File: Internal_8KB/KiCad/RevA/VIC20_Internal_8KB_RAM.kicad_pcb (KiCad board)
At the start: 2 copper layers, 70 x 60 mm, 10 parts, among them J1 UD4, J2 UE4, J3 SW, J4 Signals, U1 6264, U2 GAL16V8

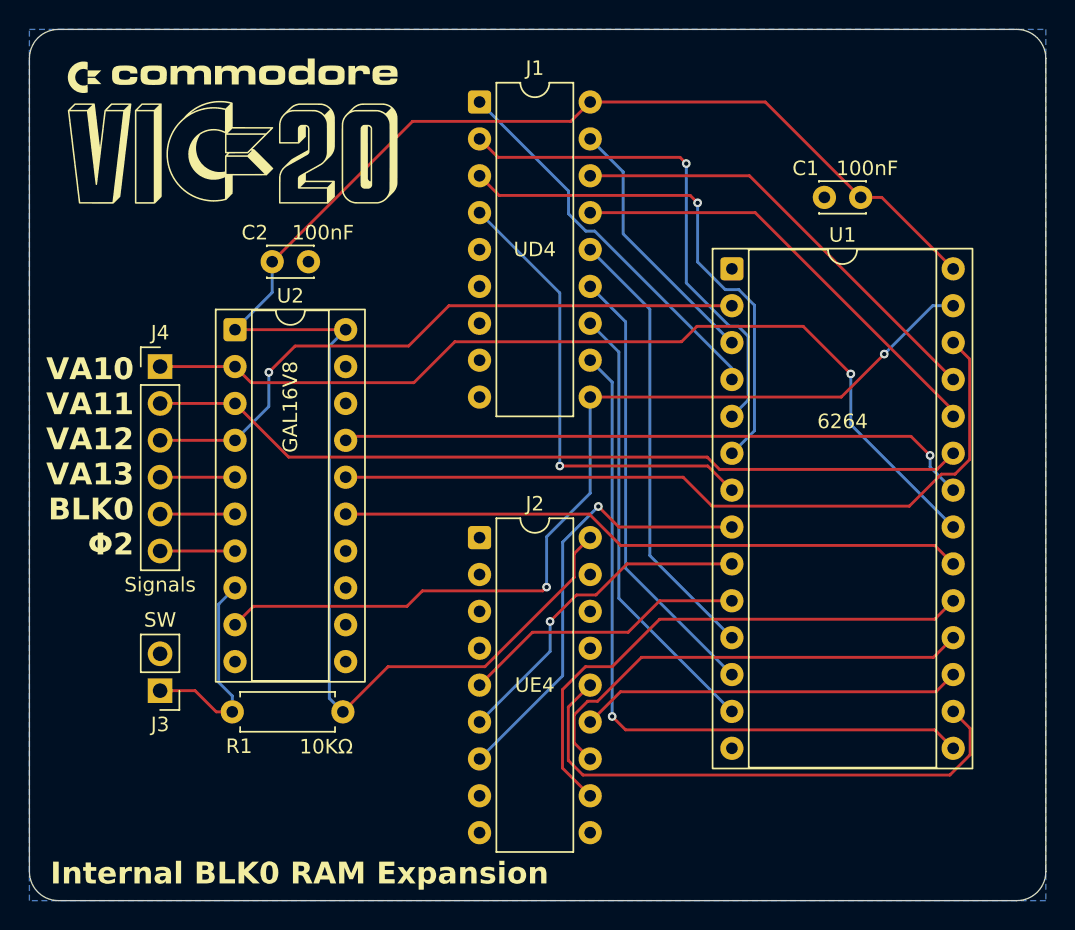
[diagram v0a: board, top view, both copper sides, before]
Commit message: Minor track routing changes
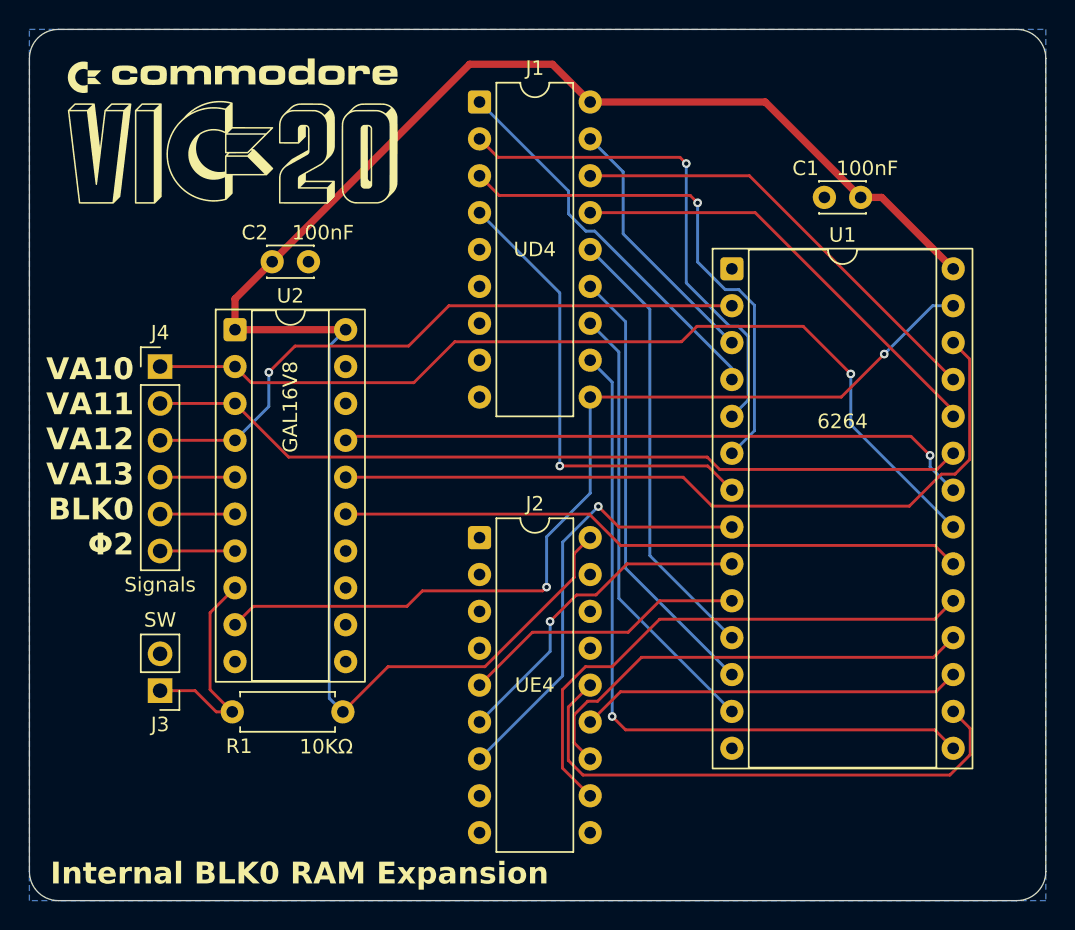
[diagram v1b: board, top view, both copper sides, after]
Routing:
- net +5V: track 119.7 -> 121.9 mm
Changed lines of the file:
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@@
 		(embedded_fonts no)
 		(model "${KICAD9_3DMODEL_DIR}/Package_DIP.3dshapes/DIP-18_W7.62mm.wrl"
+			(hide yes)
 			(offset
 				(xyz 0 0 0)
@@
 		(embedded_fonts no)
 		(model "${KICAD9_3DMODEL_DIR}/Package_DIP.3dshapes/DIP-18_W7.62mm.wrl"
+			(hide yes)
 			(offset
 				(xyz 0 0 0)
@@
 		(start 70.82 51.8)
 		(end 63.2 51.8)
-		(width 0.2)
+		(width 0.5)
 		(layer "F.Cu")
 		(net 1)
@@
 		(start 99.72 36.12)
 		(end 106.29 42.69)
-		(width 0.2)
+		(width 0.5)
+		(layer "F.Cu")
+		(net 1)
+	)
+	(segment
+		(start 63.2 51.8)
+		(end 63.2 49.68)
+		(width 0.5)
 		(layer "F.Cu")
 		(net 1)
@@
 	(segment
 		(start 87.66 36.12)
-		(end 86.326 37.454)
-		(width 0.2)
+		(end 85.06 33.52)
+		(width 0.5)
 		(layer "F.Cu")
 		(net 1)
 	)
 	(segment
-		(start 86.326 37.454)
-		(end 75.426 37.454)
-		(width 0.2)
+		(start 79.36 33.52)
+		(end 65.76 47.12)
+		(width 0.5)
+		(layer "F.Cu")
+		(net 1)
+	)
+	(segment
+		(start 63.2 49.68)
+		(end 65.76 47.12)
+		(width 0.5)
 		(layer "F.Cu")
 		(net 1)
@@
 		(start 106.29 42.69)
 		(end 107.74 42.69)
-		(width 0.2)
+		(width 0.5)
 		(layer "F.Cu")
 		(net 1)
@@
 		(start 87.66 36.12)
 		(end 99.72 36.12)
-		(width 0.2)
+		(width 0.5)
 		(layer "F.Cu")
 		(net 1)
 	)
 	(segment
-		(start 75.426 37.454)
-		(end 65.76 47.12)
-		(width 0.2)
+		(start 107.74 42.69)
+		(end 112.66 47.61)
+		(width 0.5)
 		(layer "F.Cu")
 		(net 1)
 	)
 	(segment
-		(start 107.74 42.69)
-		(end 112.66 47.61)
-		(width 0.2)
+		(start 85.06 33.52)
+		(end 79.36 33.52)
+		(width 0.5)
 		(layer "F.Cu")
 		(net 1)
@@
 	)
 	(segment
-		(start 65.76 49.24)
-		(end 63.2 51.8)
-		(width 0.2)
-		(layer "B.Cu")
-		(net 1)
-	)
-	(segment
-		(start 65.76 47.12)
-		(end 65.76 49.24)
-		(width 0.2)
-		(layer "B.Cu")
-		(net 1)
-	)
-	(segment
 		(start 95.0588 43.063)
 		(end 94.5508 42.555)
@@
 	)
 	(segment
-		(start 60.4483 76.66)
-		(end 58.04 76.66)
+		(start 63.2 69.58)
+		(end 61.48 71.3)
 		(width 0.2)
 		(layer "F.Cu")
@@
 	)
 	(segment
-		(start 61.9083 78.12)
-		(end 60.4483 76.66)
+		(start 60.4483 76.66)
+		(end 58.04 76.66)
 		(width 0.2)
 		(layer "F.Cu")
@@
 	)
 	(segment
-		(start 63.01 78.12)
-		(end 61.9083 78.12)
+		(start 61.48 76.59)
+		(end 63.01 78.12)
 		(width 0.2)
 		(layer "F.Cu")
@@
 	)
 	(segment
-		(start 62.0726 70.7074)
-		(end 63.2 69.58)
-		(width 0.2)
-		(layer "B.Cu")
-		(net 32)
-	)
-	(segment
-		(start 63.01 77.0183)
-		(end 62.0726 76.0809)
+		(start 61.9083 78.12)
+		(end 60.4483 76.66)
 		(width 0.2)
-		(layer "B.Cu")
+		(layer "F.Cu")
 		(net 32)
 	)
 	(segment
-		(start 62.0726 76.0809)
-		(end 62.0726 70.7074)
+		(start 61.48 71.3)
+		(end 61.48 76.59)
 		(width 0.2)
-		(layer "B.Cu")
+		(layer "F.Cu")
 		(net 32)
 	)
 	(segment
 		(start 63.01 78.12)
-		(end 63.01 77.0183)
+		(end 61.9083 78.12)
 		(width 0.2)
-		(layer "B.Cu")
+		(layer "F.Cu")
 		(net 32)
 	)

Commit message: Cosmetic change
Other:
- board text added: "Internal BLK0 RAM Expansion ©2025"
- board text removed: "Internal BLK0 RAM Expansion"
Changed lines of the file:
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@@
 		(layer "Edge.Cuts")
 	)
-	(gr_text "Internal BLK0 RAM Expansion"
+	(gr_text "Internal BLK0 RAM Expansion ©2025"
 		(at 50.48 90.12 0)
 		(layer "F.SilkS")
